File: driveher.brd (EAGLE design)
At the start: 50 x 24 mm, 21 parts, among them Q1 PSMN, Q2 PSMN

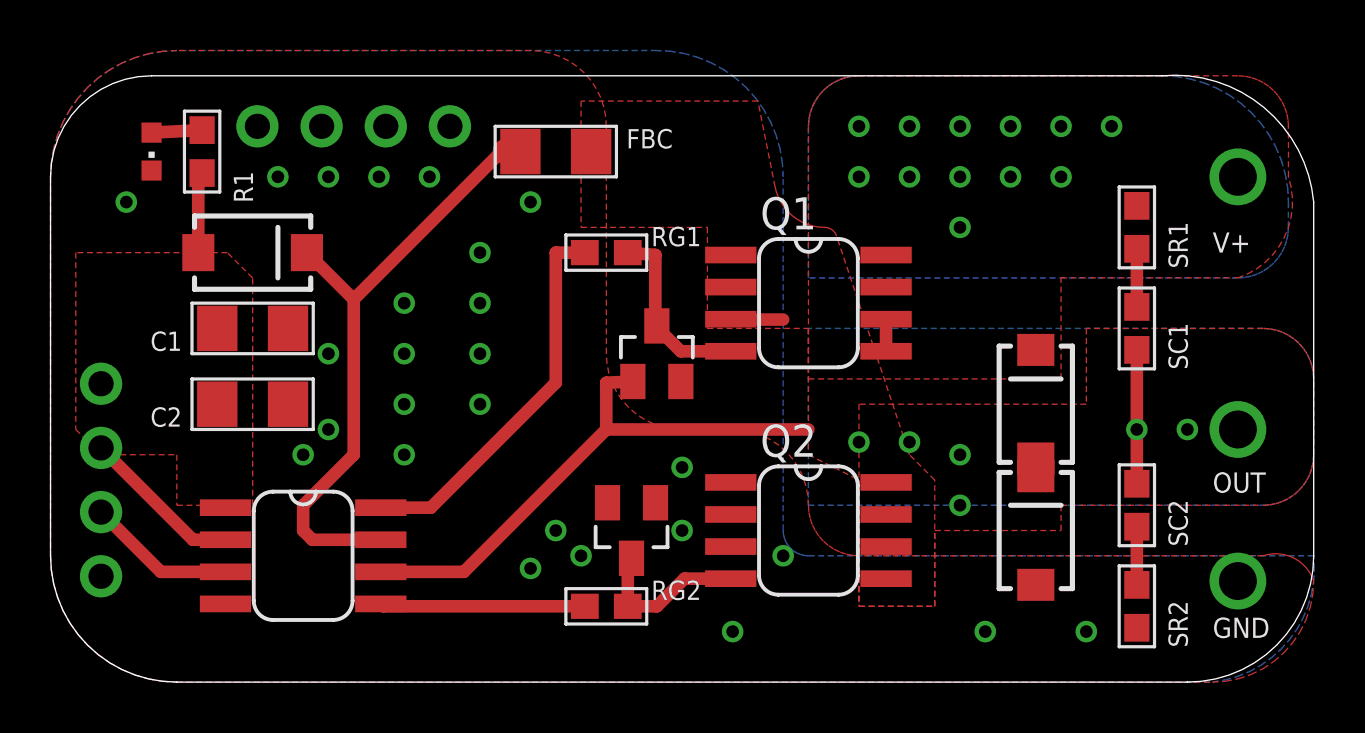
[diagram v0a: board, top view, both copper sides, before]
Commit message: fixed ir25606 / '67 routing, beefed up trace b/t high side source & output, added input protect resistors
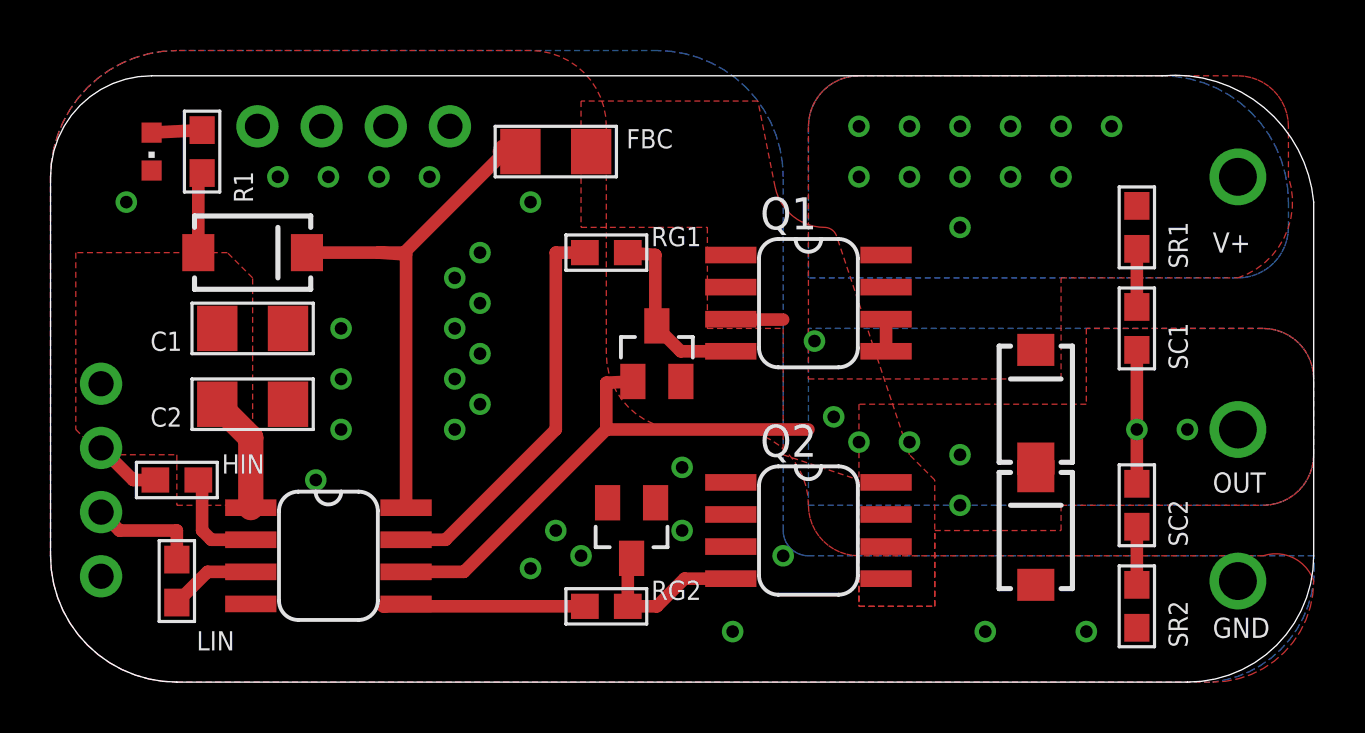
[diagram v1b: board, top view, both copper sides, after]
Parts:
- added HIN, LIN: (no value), nonolith:0603
- moved U$1 1.00 mm to (11.0, 5.00)
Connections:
- removed net HIN: JP1.3, U$1.2
- removed net LIN: JP1.2, U$1.3
- new net HIN-P: HIN.2, U$1.2
- new net LIN-P: LIN.2, U$1.3
- new net N$3: HIN.1, JP1.3
- new net N$4: JP1.2, LIN.1
- net FLOAT: now also U$1.8; no longer U$1.7
- net HOUT: now also U$1.7; no longer U$1.8
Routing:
- net HIN: track 6.43 -> 0.00 mm
- net LIN: track 5.91 -> 0.00 mm
- net 12V: track 3.21 -> 7.86 mm
- net N$4: track 0.00 -> 4.45 mm
- net HIN-P: track 0.00 -> 4.14 mm
- net FLOAT: track 24.8 -> 21.4 mm
- net LIN-P: track 0.00 -> 3.43 mm
- net N$3: track 0.00 -> 2.68 mm
- net OUT: track 28.5 -> 27.5 mm, vias 7 -> 9
- net LOUT: track 8.12 -> 8.89 mm
- net HOUT: track 15.3 -> 15.9 mm
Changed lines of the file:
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@@
 </autorouter>
 <elements>
-<element name="U$1" library="nonolith" package="SO-08" value="IRS218-67" x="10" y="5" smashed="yes" rot="R270">
-<attribute name="VALUE" x="7.968" y="1.063" size="1.27" layer="27" font="vector" ratio="12"/>
+<element name="U$1" library="nonolith" package="SO-08" value="IRS218-67" x="11" y="5" smashed="yes" rot="R270">
+<attribute name="VALUE" x="8.968" y="1.063" size="1.27" layer="27" font="vector" ratio="12"/>
 </element>
 <element name="Q1" library="nonolith" package="SO-08" value="PSMN" x="30" y="15" smashed="yes" rot="R270">
@@
 <element name="JP2" library="nonolith" package="1X04_ROUND" value="" x="12" y="22" smashed="yes">
 <attribute name="VALUE" x="6.92" y="18.825" size="1.27" layer="27"/>
+</element>
+<element name="HIN" library="nonolith" package="0603" value="" x="5" y="8"/>
+<element name="LIN" library="nonolith" package="0603" value="" x="5" y="4" smashed="yes" rot="R270">
+<attribute name="NAME" x="5.778" y="1.254" size="0.762" layer="25" font="vector" ratio="10"/>
 </element>
 </elements>
@@
 <vertex x="26" y="18"/>
 <vertex x="26" y="14"/>
-<vertex x="30" y="14"/>
-<vertex x="30" y="9"/>
+<vertex x="29" y="14"/>
+<vertex x="29" y="9"/>
 <vertex x="32" y="8"/>
 <vertex x="32" y="3"/>
@@
 <vertex x="21" y="18"/>
 </polygon>
-<wire x1="13.0734" y1="4.365" x2="16.365" y2="4.365" width="0.5" layer="1"/>
+<wire x1="14.0734" y1="4.365" x2="16.365" y2="4.365" width="0.5" layer="1"/>
 <wire x1="16.365" y1="4.365" x2="22" y2="10" width="0.5" layer="1"/>
 <wire x1="22" y1="10" x2="30" y2="10" width="0.5" layer="1"/>
 <contactref element="SC1" pad="2"/>
 <via x="47" y="10" extent="1-16" drill="1.5"/>
-<polygon width="0.5" layer="1" isolate="1.5" rank="5">
+<polygon width="0.5" layer="1" isolate="1" rank="5">
 <vertex x="50" y="9"/>
 <vertex x="50" y="12" curve="90"/>
@@
 <vertex x="48" y="7" curve="90"/>
 </polygon>
-<polygon width="0.5" layer="16" isolate="1.5">
+<polygon width="0.5" layer="16" isolate="1">
 <vertex x="30" y="7"/>
 <vertex x="48" y="7" curve="90"/>
@@
 <wire x1="43" y1="10" x2="43" y2="7.85" width="0.5" layer="1"/>
 <wire x1="28" y1="14.35" x2="29" y2="14.35" width="0.5" layer="1"/>
+<via x="31" y="10.5" extent="1-16" drill="0.5"/>
+<via x="30.24" y="13.5" extent="1-16" drill="0.5"/>
 </signal>
 <signal name="V+">
@@
 <wire x1="6" y1="20.15" x2="5.85" y2="20" width="0.5" layer="1"/>
 <wire x1="5.85" y1="20" x2="5.85" y2="17" width="0.5" layer="1"/>
-</signal>
-<signal name="LIN">
+<wire x1="7.9266" y1="6.905" x2="7.9266" y2="9.6734" width="1" layer="1"/>
+<wire x1="7.9266" y1="9.6734" x2="6.6" y2="11" width="1" layer="1"/>
+</signal>
+<signal name="LIN-P">
 <contactref element="U$1" pad="3"/>
-<contactref element="JP1" pad="2"/>
-<wire x1="6.9266" y1="4.365" x2="4.365" y2="4.365" width="0.5" layer="1"/>
-<wire x1="4.365" y1="4.365" x2="2" y2="6.73" width="0.5" layer="1"/>
-</signal>
-<signal name="HIN">
+<contactref element="LIN" pad="2"/>
+<wire x1="7.9266" y1="4.365" x2="6.215" y2="4.365" width="0.5" layer="1"/>
+<wire x1="6.215" y1="4.365" x2="5" y2="3.15" width="0.5" layer="1"/>
+</signal>
+<signal name="HIN-P">
 <contactref element="U$1" pad="2"/>
-<contactref element="JP1" pad="3"/>
-<wire x1="6.9266" y1="5.635" x2="5.635" y2="5.635" width="0.5" layer="1"/>
-<wire x1="2" y1="9.27" x2="5.635" y2="5.635" width="0.5" layer="1"/>
+<contactref element="HIN" pad="2"/>
+<wire x1="7.9266" y1="5.635" x2="6.365" y2="5.635" width="0.5" layer="1"/>
+<wire x1="6.365" y1="5.635" x2="6" y2="6" width="0.5" layer="1"/>
+<wire x1="6" y1="6" x2="6" y2="7.85" width="0.5" layer="1"/>
+<wire x1="6" y1="7.85" x2="5.85" y2="8" width="0.5" layer="1"/>
 </signal>
 <signal name="FLOAT">
 <contactref element="FBD" pad="C"/>
-<contactref element="U$1" pad="7"/>
+<contactref element="U$1" pad="8"/>
 <contactref element="FBC" pad="1"/>
-<wire x1="10.15" y1="17" x2="12" y2="15.15" width="0.5" layer="1"/>
-<wire x1="12" y1="15.15" x2="12" y2="9" width="0.5" layer="1"/>
-<wire x1="12" y1="9" x2="10" y2="7" width="0.5" layer="1"/>
-<wire x1="10" y1="7" x2="10" y2="6" width="0.5" layer="1"/>
-<wire x1="10" y1="6" x2="10.365" y2="5.635" width="0.5" layer="1"/>
-<wire x1="10.365" y1="5.635" x2="13.0734" y2="5.635" width="0.5" layer="1"/>
 <wire x1="18.6" y1="21" x2="18" y2="21" width="1" layer="1"/>
 <wire x1="18" y1="21" x2="17.85" y2="21" width="0.5" layer="1"/>
-<wire x1="17.85" y1="21" x2="12" y2="15.15" width="0.5" layer="1"/>
+<wire x1="10.15" y1="17" x2="13" y2="17" width="0.5" layer="1"/>
+<wire x1="13" y1="17" x2="14" y2="17" width="0.5" layer="1"/>
+<wire x1="14" y1="17" x2="18" y2="21" width="0.5" layer="1"/>
+<wire x1="14.0734" y1="6.905" x2="14.0734" y2="16.9266" width="0.5" layer="1"/>
+<wire x1="14.0734" y1="16.9266" x2="13" y2="17" width="0.5" layer="1"/>
 </signal>
 <signal name="GND">
@@
 <via x="17" y="13" extent="1-16" drill="0.5"/>
 <via x="17" y="11" extent="1-16" drill="0.5"/>
-<via x="14" y="15" extent="1-16" drill="0.5"/>
-<via x="14" y="13" extent="1-16" drill="0.5"/>
-<via x="14" y="11" extent="1-16" drill="0.5"/>
+<via x="16" y="16" extent="1-16" drill="0.5"/>
+<via x="16" y="14" extent="1-16" drill="0.5"/>
+<via x="16" y="12" extent="1-16" drill="0.5"/>
 <via x="19" y="4.5" extent="1-16" drill="0.5"/>
 <via x="25" y="8.5" extent="1-16" drill="0.5"/>
 <contactref element="D2" pad="1"/>
 <via x="21" y="5" extent="1-16" drill="0.5"/>
-<via x="14" y="9" extent="1-16" drill="0.5"/>
+<via x="16" y="10" extent="1-16" drill="0.5"/>
 <via x="15" y="20" extent="1-16" drill="0.5"/>
 <via x="3" y="19" extent="1-16" drill="0.5"/>
-<via x="11" y="13" extent="1-16" drill="0.5"/>
-<via x="11" y="10" extent="1-16" drill="0.5"/>
-<via x="10" y="9" extent="1-16" drill="0.5"/>
+<via x="11.5" y="14" extent="1-16" drill="0.5"/>
 <contactref element="JP2" pad="4"/>
 <contactref element="JP2" pad="3"/>
@@
 <contactref element="JP2" pad="1"/>
 <via x="29" y="5" extent="1-16" drill="0.5"/>
+<via x="11.5" y="12" extent="1-16" drill="0.5"/>
+<via x="11.5" y="10" extent="1-16" drill="0.5"/>
+<via x="10.5" y="8" extent="1-16" drill="0.5"/>
 </signal>
 <signal name="P2">
@@
 </signal>
 <signal name="HOUT">
-<contactref element="U$1" pad="8"/>
+<contactref element="U$1" pad="7"/>
 <contactref element="RG1" pad="1"/>
-<wire x1="13.0734" y1="6.905" x2="15.055" y2="6.905" width="0.5" layer="1"/>
-<wire x1="15.055" y1="6.905" x2="20" y2="11.85" width="0.5" layer="1"/>
-<wire x1="20" y1="11.85" x2="20" y2="17" width="0.5" layer="1"/>
+<wire x1="20" y1="10" x2="20" y2="17" width="0.5" layer="1"/>
 <wire x1="20" y1="17" x2="21.15" y2="17" width="0.5" layer="1"/>
+<wire x1="14.0734" y1="5.635" x2="15.635" y2="5.635" width="0.5" layer="1"/>
+<wire x1="15.635" y1="5.635" x2="20" y2="10" width="0.5" layer="1"/>
 </signal>
 <signal name="LOUT">
 <contactref element="U$1" pad="5"/>
 <contactref element="RG2" pad="1"/>
-<wire x1="13.0734" y1="3.095" x2="13.1684" y2="3" width="0.5" layer="1"/>
+<wire x1="14.0734" y1="3.095" x2="13.1684" y2="3" width="0.5" layer="1"/>
 <wire x1="13.1684" y1="3" x2="21.15" y2="3" width="0.5" layer="1"/>
 </signal>
@@
 <wire x1="43" y1="17.15" x2="43" y2="14.85" width="0.5" layer="1"/>
 </signal>
+<signal name="N$3">
+<contactref element="JP1" pad="3"/>
+<contactref element="HIN" pad="1"/>
+<wire x1="4.15" y1="8" x2="3.27" y2="8" width="0.5" layer="1"/>
+<wire x1="3.27" y1="8" x2="2" y2="9.27" width="0.5" layer="1"/>
+</signal>
+<signal name="N$4">
+<contactref element="JP1" pad="2"/>
+<contactref element="LIN" pad="1"/>
+<wire x1="5" y1="4.85" x2="5" y2="6" width="0.5" layer="1"/>
+<wire x1="5" y1="6" x2="2.73" y2="6" width="0.5" layer="1"/>
+<wire x1="2.73" y1="6" x2="2" y2="6.73" width="0.5" layer="1"/>
+</signal>
 </signals>
